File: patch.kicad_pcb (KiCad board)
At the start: 2 copper layers, 65.2 x 59.2 mm, 18 parts, among them J1 Conn_01x16, Q1 NMOS, U1 74AHC1G08

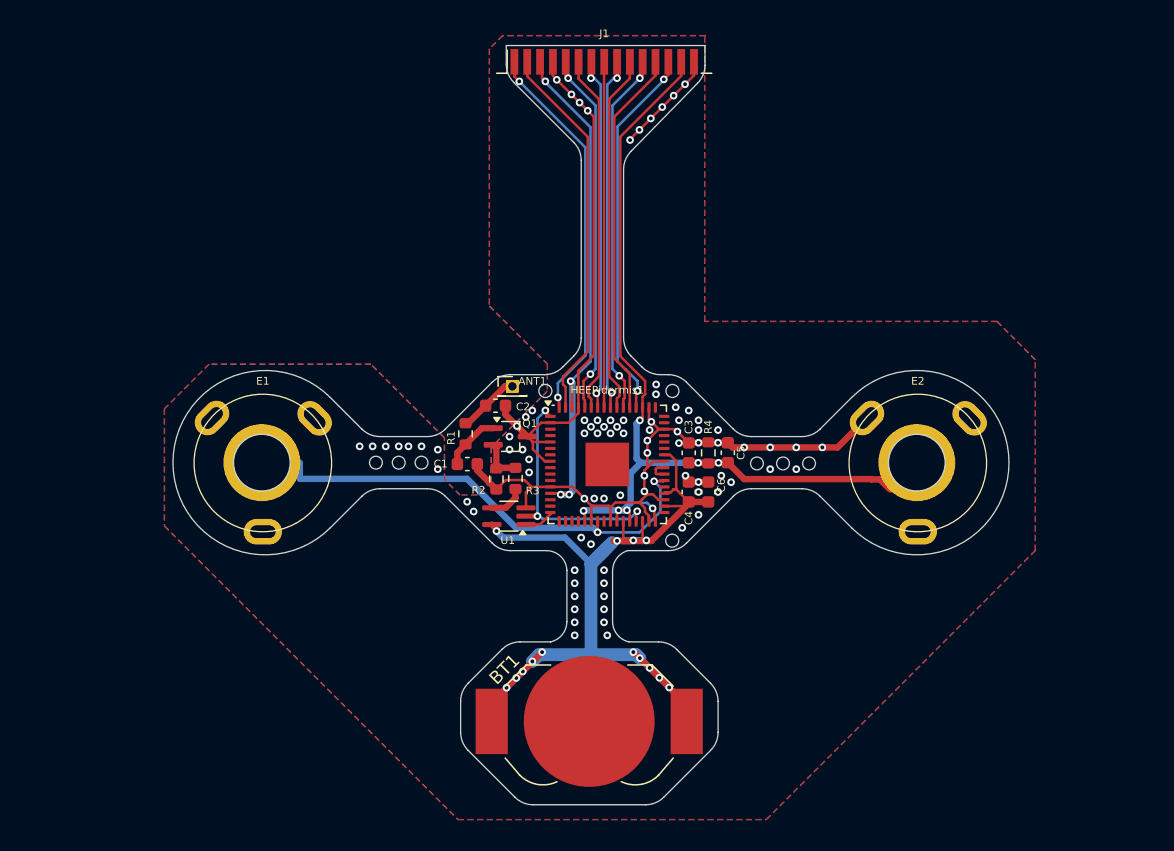
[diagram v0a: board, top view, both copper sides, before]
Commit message: Need to fix rst, ldo vbat and check parity
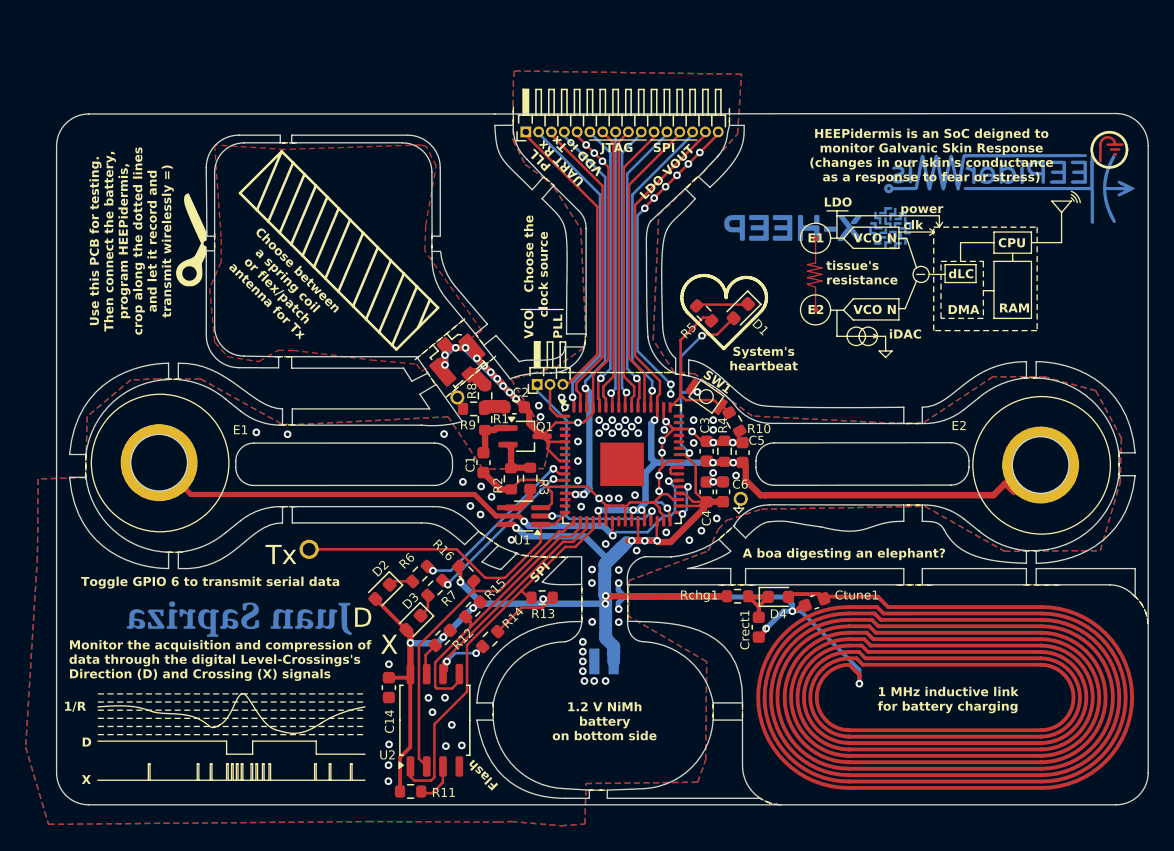
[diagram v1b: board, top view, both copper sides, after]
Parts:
- removed ANT1: Conn_01x03, Connector_PinHeader_1.27mm:PinHeader_1x01_P1.27mm_Vertical
- added C14: 100n, Capacitor_SMD:C_0603_1608Metric, F.Cu at (91.4, 82.8)
- added Crect1: 1u, Capacitor_SMD:C_0603_1608Metric, F.Cu at (120.3, 78.1)
- added Ctune1: 10u, Capacitor_SMD:C_0603_1608Metric, F.Cu at (124.6, 76.2)
- added D1: LED, LED_SMD:LED_0603_1608Metric, F.Cu at (118.9, 53.5)
- added D2: LED, LED_SMD:LED_0603_1608Metric, F.Cu at (90.9, 75.3)
- added D3: LED, LED_SMD:LED_0603_1608Metric, F.Cu at (93.4, 77.8)
- added D4: D_Schottky, Diode_SMD:D_0603_1608Metric, F.Cu at (121.8, 75.7)
- added G***: LOGO, LOGO, F.Cu at (75.9, 47.9)
- added G*** (x2): LOGO, LOGO, B.Cu at (124.8, 47.0)
- added G*** (x2): LOGO, LOGO, B.Cu at (79.7, 78.4)
- added G***: LOGO, LOGO, B.Cu at (86.0, 43.4)
- added G*** (x2): LOGO, LOGO, B.Cu at (138.9, 43.9)
- added J2: Conn_01x16, Connector_PinHeader_1.00mm:PinHeader_1x16_P1.00mm_Horizontal, F.Cu at (102.1, 39.5)
- added J3: Conn_Coaxial_Small, Connector_Coaxial:U.FL_Molex_MCRF_73412-0110_Vertical, F.Cu at (96.8, 57.3)
- added J4: Conn_01x01, Connector_PinHeader_2.54mm:PinHeader_1x01_P2.54mm_Vertical, F.Cu at (96.8, 60.2)
- added J5: Conn_01x01, Connector_PinHeader_2.54mm:PinHeader_1x01_P2.54mm_Vertical, F.Cu at (85.2, 72.0)
- added J6: Conn_01x01, Connector_PinHeader_2.54mm:PinHeader_1x01_P2.54mm_Vertical, F.Cu at (118.9, 68.1)
- added NT1: NetTie_2, libs:1MHz_coil_29x14, F.Cu at (134.2, 84.1)
- added R10: 10k, Resistor_SMD:R_0603_1608Metric, F.Cu at (118.4, 62.1)
- added R11: 10k, Resistor_SMD:R_0603_1608Metric, F.Cu at (93.1, 90.9)
- added R12: 10k, Resistor_SMD:R_0603_1608Metric, F.Cu at (95.6, 78.9)
- added R13: 10k, Resistor_SMD:R_0603_1608Metric, F.Cu at (103.4, 75.8)
- added R14: 10k, Resistor_SMD:R_0603_1608Metric, F.Cu at (99.3, 79.0)
- added R15: 10k, Resistor_SMD:R_0603_1608Metric, F.Cu at (98.0, 76.7)
- added R16: 10k, Resistor_SMD:R_0603_1608Metric, F.Cu at (97.5, 73.9)
- added R5: 330, Resistor_SMD:R_0603_1608Metric, F.Cu at (116.0, 53.6)
- added R6: 330, Resistor_SMD:R_0603_1608Metric, F.Cu at (93.9, 74.0)
- added R7: 330, Resistor_SMD:R_0603_1608Metric, F.Cu at (95.1, 75.0)
- added R8: 0R, Resistor_SMD:R_0603_1608Metric, F.Cu at (98.9, 60.1)
- added R9: 0R, Resistor_SMD:R_0603_1608Metric, F.Cu at (98.0, 61.1)
- added REF**: ESL, libs:ESL, B.Cu at (86.3, 56.3)
- added Rchg1: 1k, Resistor_SMD:R_0603_1608Metric, F.Cu at (118.6, 75.7)
- added SW1: SW_SPST, libs:SPST_1.6x3mm, F.Cu at (116.2, 60.1)
- added U2: W25Q12NEZPIG, Package_SO:SOIC-8_5.23x5.23mm_P1.27mm, F.Cu at (95.0, 85.4)
- BT1: footprint Battery:BatteryHolder_LINX_BAT-HLD-012-SMT -> Battery:BatteryHolder_Seiko_MS621F; moved to B.Cu
- J1: value Conn_01x16 -> Conn_01x03; footprint Connector_FFC-FPC:TE_1-84952-5_1x15-1MP_P1.0mm_Horizontal -> Connector_PinHeader_1.00mm:PinHeader_1x03_P1.00mm_Horizontal
- R1: value ~ -> 0R
- R2: value 1M -> 100k
- moved J1 23.9 mm to (103.0, 59.2), turned to 90 degrees
- moved E2 9.65 mm to (142.2, 65.5)
- moved E1 8.01 mm to (73.5, 65.3)
- moved BT1 4.82 mm to (108.2, 80.8), turned to 90 degrees
- moved R1 1.89 mm to (98.9, 61.9)
- moved C2 1.47 mm to (101.2, 61.0)
- moved C3 1.40 mm to (116.2, 64.4)
- moved C4 1.40 mm to (116.2, 67.6)
- moved R4 1.28 mm to (117.6, 64.4)
- moved C1 1.26 mm to (98.8, 65.3), turned to 90 degrees
- moved C5 1.15 mm to (119.0, 64.5)
- moved HEEPidermis1 1.15 mm to (109.6, 65.4)
- moved Q1 1.15 mm to (102.0, 63.2)
- moved R3 1.15 mm to (102.4, 66.5)
- moved C6 1.15 mm to (117.5, 67.6)
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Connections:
- HEEPidermis1 pad 1: /VCO_P_VN0 -> Net-(J1-Pin_2)
- HEEPidermis1 pad 49: unconnected-(HEEPidermis1-Pad49) -> Net-(SW1-A)
- J1 pad 1: /UART.RX -> /VCO_P_VN0
- J1 pad 2: /UART.TX -> Net-(J1-Pin_2)
- J1 pad 3: /SUPPLY_IO_VDD -> /PLL_clk
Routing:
- net GND: track 101.6 -> 149.9 mm, vias 89 -> 104
- net /LDO_VBAT: track 78.5 -> 122.1 mm
- net /SPI_CS: track 0.00 -> 29.5 mm
- net /SPI_MISO: track 0.00 -> 26.6 mm
- net /PLL_clk: track 0.00 -> 23.3 mm
- net /Tx: track 2.36 -> 24.5 mm
- net /SPI_MOSI: track 0.00 -> 21.7 mm
- net /SPI_SCK: track 0.00 -> 21.4 mm, vias 0 -> 2
- net /LC_DIR_GPIO_2: track 0.00 -> 14.4 mm, vias 0 -> 2
- net Net-(SW1-A): track 0.00 -> 13.2 mm
- net /LC_XING_GPIO_3: track 0.00 -> 12.6 mm, vias 0 -> 2
- net /VCO_N_VIN: track 36.0 -> 44.9 mm, vias 2 -> 3
- net /ANT: track 0.00 -> 7.75 mm
- net /SUPPLY_IO_VDD: track 40.4 -> 34.2 mm, vias 4 -> 3
- net /JTAG.TDI: track 27.6 -> 21.7 mm, vias 2 -> 1
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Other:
- board size 65.2 x 59.2 mm -> 85.1 x 53.9 mm
- board text added: "1 MHz inductive link for battery charging"
- board text added: "1.2 V NiMh battery on bottom side"
- board text added: "1/R"
- board text added: "A boa digesting an elephant?"
- board text added: "CPU"
- board text added: "Choose between a spring coil or flex/patch antenna for Tx"
- board text added: "D"
- board text added: "DMA"
- board text added: "E1"
- board text added: "E2"
- board text added: "Flash"
- board text added: "HEEPidermis is an SoC deigned to monitor Galvanic Skin Response (changes in our skin's conductance as a response to fear or stress)"
- board text added: "JTAG"
- board text added: "LDO"
- board text added: "LDO VOUT"
- board text added: "Monitor the acquisition and compression of data through the digital Level-Crossings's Direction (D) and Crossing (X) signals"
- board text added: "PLL"
- board text added: "RAM"
- board text added: "SPI"
- board text added: "System's heartbeat"
- board text added: "The LDO generates 0.8V to - bias the tissue - supply the MCU"
- board text added: "The VCO N reads the tissue's voltage to get the drop from the current drained by the 8-bit iDAC"
- board text added: "The VCO P reads the battery level to: - monitor battery charge - generate the system clock - generate a sub-carrier for load-modulation - use as reference for pseudo-differential mode"
- board text added: "Toggle GPIO 6 to transmit serial data"
- board text added: "Tx"
- board text added: "UART Rx"
- board text added: "Use this PCB for testing. Then connect the battery, program HEEPidermis, crop along the dotted lines and let it record and transmit wirelessly =)"
- board text added: "VCO Choose the clock source PLL"
- board text added: "VCO N"
- board text added: "VDD io"
- board text added: "X"
- board text added: "clk"
- board text added: "dLC"
- board text added: "iDAC"
- board text added: "power"
- board text added: "tissue's resistance"

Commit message: Corrected connection
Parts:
- R10: value 10k -> 100k
- moved J1 0.19 mm to (102.8, 59.2)
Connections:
- HEEPidermis1 pad 13: /SUPPLY_IO_VDD -> /LDO_VBAT
- HEEPidermis1 pad 62: /SUPPLY_IO_VDD -> /LDO_VBAT
- J2 pad 2: /UART.RX -> /nRST
- J2 pad 3: /UART.TX -> /UART.RX
- J2 pad 4: /SUPPLY_IO_VDD -> /UART.TX
- J2 pad 5: GND -> /LDO_VBAT
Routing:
- net /LDO_VBAT: track 122.1 -> 167.3 mm, vias 14 -> 17
- net /SUPPLY_IO_VDD: track 34.2 -> 0.00 mm, vias 3 -> 0
- net /nRST: track 0.00 -> 27.7 mm, vias 0 -> 1
- net GND: track 149.9 -> 127.4 mm, vias 104 -> 99
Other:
- board text added: "HEEPidermis is an SoC designed to monitor Galvanic Skin Response (changes in our skin's conductance as a response to fear or stress)"
- board text added: "SPIs"
- board text added: "Vbat/io"
- board text removed: "HEEPidermis is an SoC deigned to monitor Galvanic Skin Response (changes in our skin's conductance as a response to fear or stress)"
- board text removed: "VDD io"
